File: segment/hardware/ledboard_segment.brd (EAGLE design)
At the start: 21.8 x 21.8 mm, 13 parts, among them J1 ISP, U1 ATMEGA328P_TQFP, Y1 16MHz

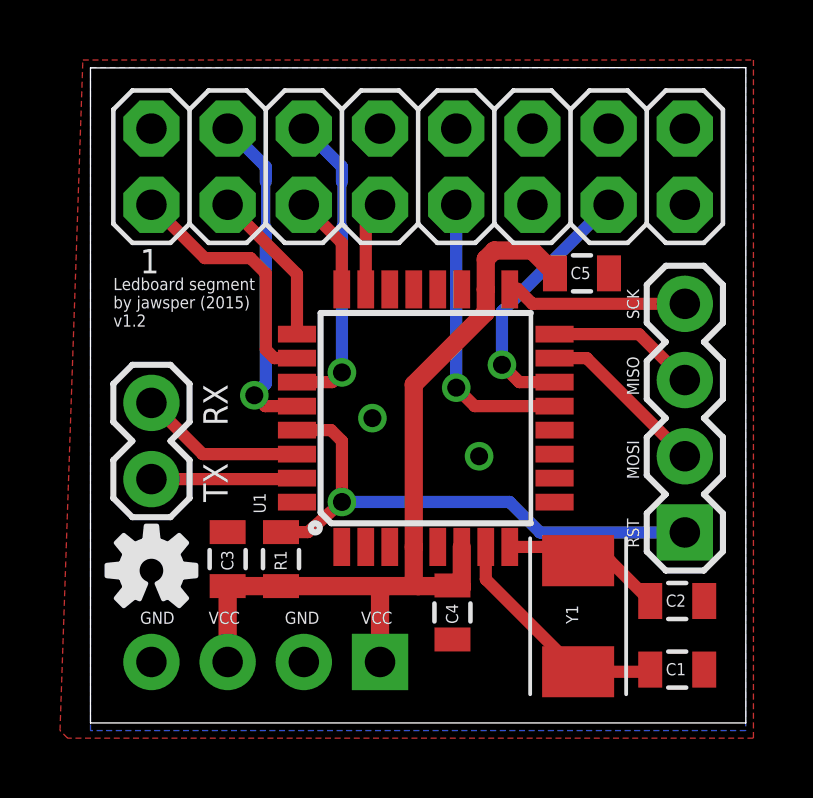
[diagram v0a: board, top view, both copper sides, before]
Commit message: Minor tweaks, board version 1.2
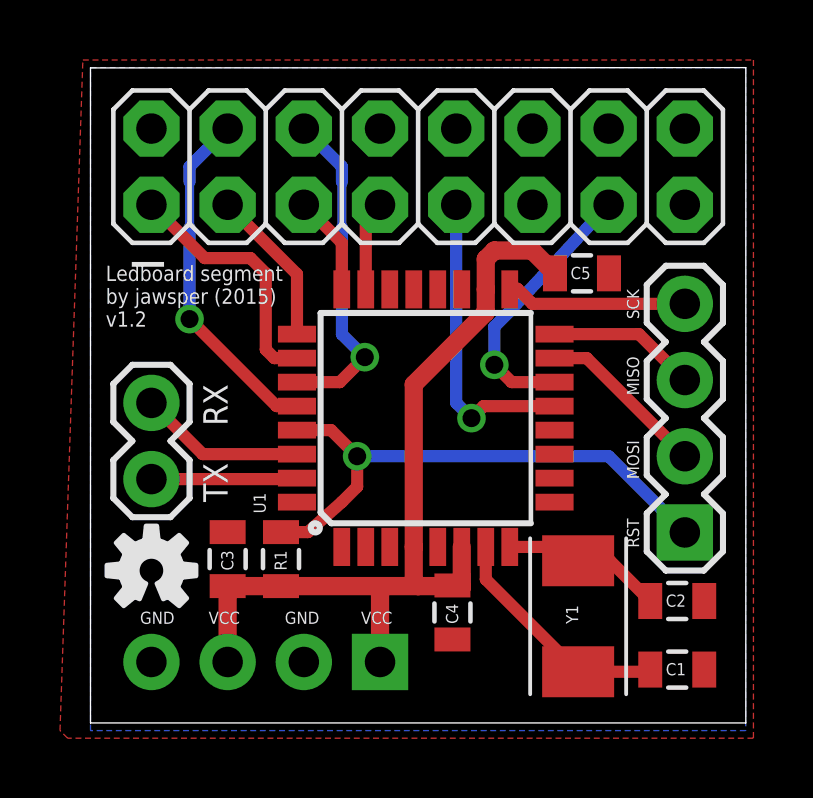
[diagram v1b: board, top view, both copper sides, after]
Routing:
- net OE: track 10.3 -> 11.1 mm
- net UDAT: track 9.63 -> 10.3 mm
- net RESET: track 17.9 -> 18.5 mm
- net STROBE: track 11.1 -> 11.7 mm
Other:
- board text added: "_"
- board text removed: "1"
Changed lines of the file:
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@@
 <layer number="46" name="Milling" color="3" fill="1" visible="no" active="yes"/>
 <layer number="47" name="Measures" color="7" fill="1" visible="no" active="yes"/>
-<layer number="48" name="Document" color="7" fill="1" visible="no" active="yes"/>
+<layer number="48" name="Document" color="7" fill="1" visible="yes" active="yes"/>
 <layer number="49" name="Reference" color="7" fill="1" visible="no" active="yes"/>
 <layer number="50" name="dxf" color="7" fill="1" visible="no" active="no"/>
@@
 <layer number="113" name="IDFDebug" color="4" fill="1" visible="no" active="yes"/>
 <layer number="116" name="Patch_BOT" color="9" fill="4" visible="no" active="yes"/>
-<layer number="121" name="_tsilk" color="7" fill="1" visible="yes" active="yes"/>
-<layer number="122" name="_bsilk" color="7" fill="1" visible="yes" active="yes"/>
+<layer number="121" name="_tsilk" color="7" fill="1" visible="no" active="yes"/>
+<layer number="122" name="_bsilk" color="7" fill="1" visible="no" active="yes"/>
 <layer number="123" name="tTestmark" color="7" fill="1" visible="no" active="yes"/>
 <layer number="124" name="bTestmark" color="7" fill="1" visible="no" active="yes"/>
@@
 <text x="6.858" y="61.976" size="0.8128" layer="25" rot="R90">TX</text>
 <text x="6.858" y="64.516" size="0.8128" layer="25" rot="R90">RX</text>
-<text x="3.937" y="69.596" size="0.8128" layer="25">1</text>
+<text x="3.683" y="70.358" size="1.6764" layer="25" font="vector">_</text>
 <text x="20.574" y="60.452" size="0.4064" layer="25" rot="R90">RST</text>
 <text x="20.574" y="62.738" size="0.4064" layer="25" rot="R90">MOSI</text>
@@
 <text x="6.223" y="57.912" size="0.4064" layer="25">VCC</text>
 <text x="11.303" y="57.912" size="0.4064" layer="25">VCC</text>
-<text x="3.048" y="67.818" size="0.4064" layer="25">Ledboard segment
+<text x="2.794" y="67.818" size="0.508" layer="25" font="vector">Ledboard segment
 by jawsper (2015)
 v1.2</text>
-<dimension x1="2.286" y1="54.61" x2="24.13" y2="54.61" x3="13.208" y3="50.038" textsize="1.778" layer="20"/>
-<dimension x1="24.13" y1="54.61" x2="24.13" y2="76.454" x3="28.956" y3="65.532" textsize="1.778" layer="20"/>
+<dimension x1="2.286" y1="54.61" x2="24.13" y2="54.61" x3="13.208" y3="50.038" textsize="1.778" layer="48"/>
+<dimension x1="24.13" y1="54.61" x2="24.13" y2="76.454" x3="28.702" y3="65.532" textsize="1.778" layer="48"/>
 </plain>
 <attributes>
@@
 <contactref element="JP2" pad="4"/>
 <contactref element="JP2" pad="2"/>
-<via x="11.684" y="64.77" extent="1-16" drill="0.6"/>
-<via x="15.24" y="63.5" extent="1-16" drill="0.6"/>
 </signal>
 <signal name="LDAT">
 <contactref element="U$1" pad="13"/>
 <contactref element="U1" pad="14"/>
-<wire x1="17.7546" y1="65.97" x2="16.58" y2="65.97" width="0.4064" layer="1"/>
-<wire x1="16.58" y1="65.97" x2="16.002" y2="66.548" width="0.4064" layer="1"/>
-<via x="16.002" y="66.548" extent="1-16" drill="0.6"/>
-<wire x1="16.002" y1="66.548" x2="16.002" y2="68.326" width="0.4064" layer="16"/>
-<wire x1="16.002" y1="68.326" x2="19.558" y2="71.882" width="0.4064" layer="16"/>
+<wire x1="17.7546" y1="65.97" x2="16.326" y2="65.97" width="0.4064" layer="1"/>
+<wire x1="16.256" y1="68.326" x2="19.558" y2="71.882" width="0.4064" layer="16"/>
+<wire x1="16.326" y1="65.97" x2="15.748" y2="66.548" width="0.4064" layer="1"/>
+<via x="15.748" y="66.548" extent="1-16" drill="0.6"/>
+<wire x1="15.748" y1="66.548" x2="15.748" y2="67.818" width="0.4064" layer="16"/>
+<wire x1="15.748" y1="67.818" x2="16.256" y2="68.326" width="0.4064" layer="16"/>
 </signal>
 <signal name="UDAT">
 <contactref element="U$1" pad="9"/>
 <contactref element="U1" pad="13"/>
-<via x="14.478" y="65.786" extent="1-16" drill="0.6"/>
-<wire x1="14.478" y1="65.786" x2="14.478" y2="71.882" width="0.4064" layer="16"/>
-<wire x1="17.7546" y1="65.17" x2="15.094" y2="65.17" width="0.4064" layer="1"/>
-<wire x1="15.094" y1="65.17" x2="14.478" y2="65.786" width="0.4064" layer="1"/>
+<wire x1="14.478" y1="65.278" x2="14.478" y2="71.882" width="0.4064" layer="16"/>
+<wire x1="14.478" y1="65.278" x2="14.986" y2="64.77" width="0.4064" layer="16"/>
+<via x="14.986" y="64.77" extent="1-16" drill="0.6"/>
+<wire x1="14.986" y1="64.77" x2="15.386" y2="65.17" width="0.4064" layer="1"/>
+<wire x1="15.386" y1="65.17" x2="17.7546" y2="65.17" width="0.4064" layer="1"/>
 </signal>
 <signal name="A2">
@@
 <contactref element="U$1" pad="4"/>
 <contactref element="U1" pad="28"/>
-<wire x1="9.1694" y1="65.17" x2="8.109" y2="65.17" width="0.4064" layer="1"/>
-<wire x1="8.109" y1="65.17" x2="7.747" y2="65.532" width="0.4064" layer="1"/>
-<via x="7.747" y="65.532" extent="1-16" drill="0.6"/>
-<wire x1="8.128" y1="71.12" x2="8.128" y2="72.644" width="0.3048" layer="16"/>
-<wire x1="8.128" y1="72.644" x2="8.128" y2="73.152" width="0.4064" layer="16"/>
-<wire x1="8.128" y1="73.152" x2="6.858" y2="74.422" width="0.4064" layer="16"/>
-<wire x1="8.128" y1="71.12" x2="8.128" y2="65.913" width="0.4064" layer="16"/>
-<wire x1="8.128" y1="65.913" x2="7.747" y2="65.532" width="0.4064" layer="16"/>
+<wire x1="9.1694" y1="65.17" x2="8.49" y2="65.17" width="0.4064" layer="1"/>
+<wire x1="8.49" y1="65.17" x2="5.588" y2="68.072" width="0.4064" layer="1"/>
+<via x="5.588" y="68.072" extent="1-16" drill="0.6"/>
+<wire x1="5.588" y1="68.072" x2="5.588" y2="71.12" width="0.4064" layer="16"/>
+<wire x1="5.588" y1="71.12" x2="5.588" y2="72.644" width="0.3048" layer="16"/>
+<wire x1="5.588" y1="72.644" x2="5.588" y2="73.152" width="0.4064" layer="16"/>
+<wire x1="5.588" y1="73.152" x2="6.858" y2="74.422" width="0.4064" layer="16"/>
 </signal>
 <signal name="OE">
@@
 <wire x1="10.668" y1="73.152" x2="10.668" y2="72.644" width="0.4064" layer="16"/>
 <wire x1="10.668" y1="72.644" x2="10.668" y2="71.12" width="0.3048" layer="16"/>
-<wire x1="10.668" y1="71.12" x2="10.668" y2="66.294" width="0.4064" layer="16"/>
-<via x="10.668" y="66.294" extent="1-16" drill="0.6"/>
-<wire x1="10.668" y1="66.294" x2="10.344" y2="65.97" width="0.4064" layer="1"/>
-<wire x1="9.1694" y1="65.97" x2="10.344" y2="65.97" width="0.4064" layer="1"/>
+<wire x1="10.668" y1="71.12" x2="10.668" y2="67.564" width="0.4064" layer="16"/>
+<wire x1="9.1694" y1="65.97" x2="10.598" y2="65.97" width="0.4064" layer="1"/>
+<wire x1="10.598" y1="65.97" x2="11.43" y2="66.802" width="0.4064" layer="1"/>
+<via x="11.43" y="66.802" extent="1-16" drill="0.6"/>
+<wire x1="11.43" y1="66.802" x2="10.668" y2="67.564" width="0.4064" layer="16"/>
 </signal>
 <signal name="VCC">
@@
 <contactref element="J1" pad="1"/>
 <wire x1="9.1694" y1="64.37" x2="10.306" y2="64.37" width="0.4064" layer="1"/>
-<wire x1="10.306" y1="64.37" x2="10.668" y2="64.008" width="0.4064" layer="1"/>
-<wire x1="10.668" y1="64.008" x2="10.668" y2="61.976" width="0.4064" layer="1"/>
-<via x="10.668" y="61.976" extent="1-16" drill="0.6"/>
-<wire x1="10.668" y1="61.976" x2="16.256" y2="61.976" width="0.4064" layer="16"/>
-<wire x1="22.098" y1="60.96" x2="17.272" y2="60.96" width="0.4064" layer="16"/>
-<wire x1="17.272" y1="60.96" x2="16.256" y2="61.976" width="0.4064" layer="16"/>
 <wire x1="8.636" y1="60.971" x2="9.536" y2="60.971" width="0.4064" layer="1"/>
 <wire x1="9.536" y1="60.971" x2="10.668" y2="61.976" width="0.4064" layer="1"/>
+<via x="11.176" y="63.5" extent="1-16" drill="0.6"/>
+<wire x1="11.176" y1="63.5" x2="10.306" y2="64.37" width="0.4064" layer="1"/>
+<wire x1="10.668" y1="61.976" x2="11.176" y2="62.484" width="0.4064" layer="1"/>
+<wire x1="11.176" y1="62.484" x2="11.176" y2="63.5" width="0.4064" layer="1"/>
+<wire x1="11.176" y1="63.5" x2="19.558" y2="63.5" width="0.4064" layer="16"/>
+<wire x1="19.558" y1="63.5" x2="22.098" y2="60.96" width="0.4064" layer="16"/>
 </signal>
 <signal name="N$3">
